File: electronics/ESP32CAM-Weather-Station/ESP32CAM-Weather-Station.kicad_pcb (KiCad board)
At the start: 4 copper layers, 100 x 100 mm, 93 parts, among them IC1 BME688, IC2 SGP41-D-R4, IC3 VEML7700-TT, IC4 BQ24093DGQR, IC5 BQ29707DSET, IC6 MCP3426A0T-E_SN, IC7 TPS63070RNMR, J1 B4B-PH-SM4-TB_LF__SN_, J10 Conn_01x02_Pin, J2 B4B-PH-SM4-TB_LF__SN_, J3 B4B-PH-SM4-TB_LF__SN_, J4 B4B-PH-SM4-TB_LF__SN_, J6 XT30UPB-M, J7 Conn_01x02_Pin, J8 Conn_01x02_Pin, J9 Conn_01x02_Pin, Q2 CSD16406Q3, Q3 CSD16406Q3, U1 ESP32-CAM, U2 TPS631000DRLR, U3 GDT25-07-S1-RP

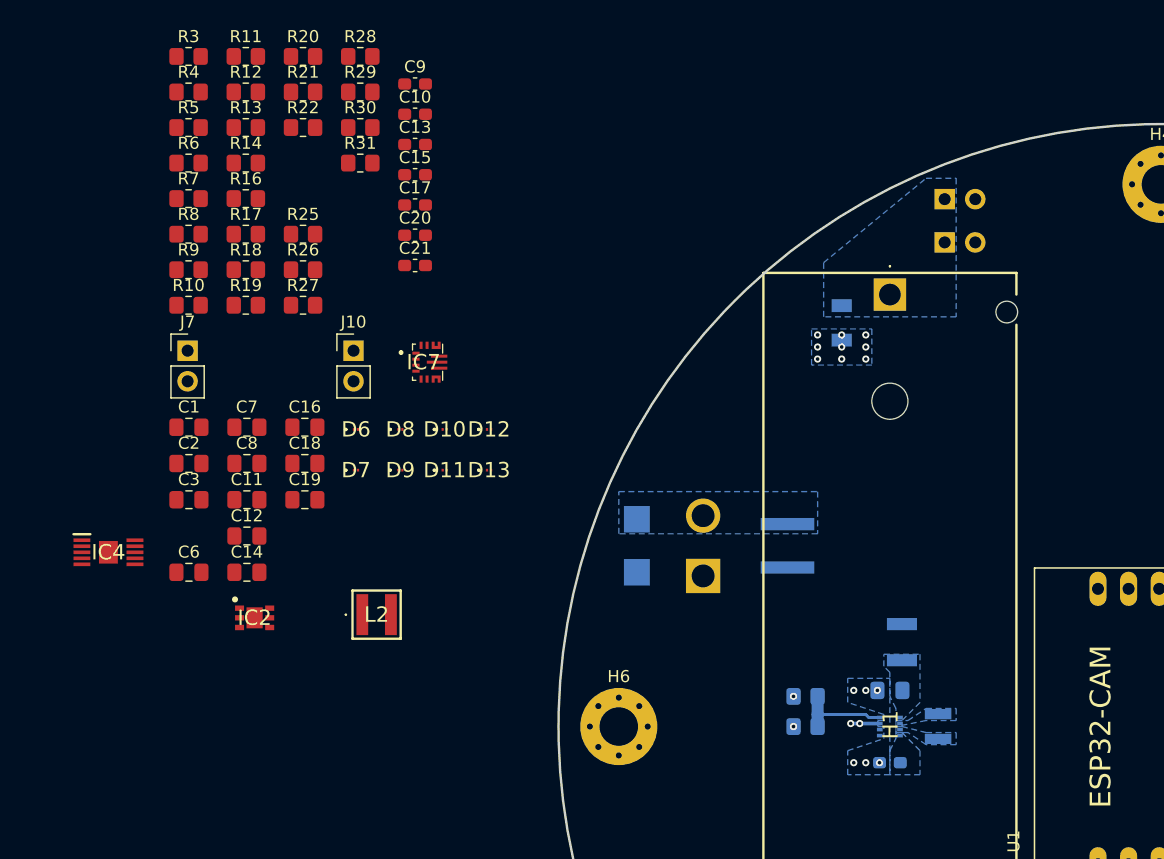
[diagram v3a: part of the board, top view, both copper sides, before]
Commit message: [WIP] Placed basic 5V regulator parts and moved 3V3 regulator so that output connects to the 3V3 plane.
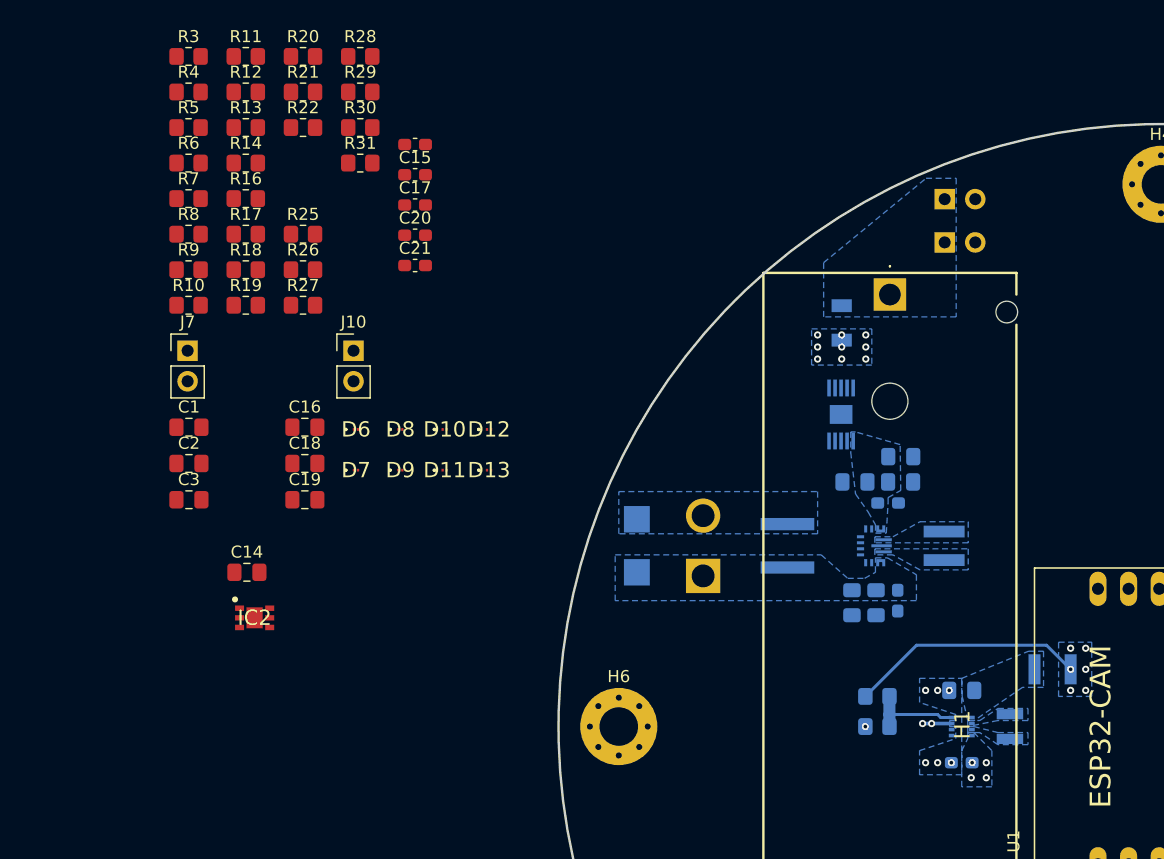
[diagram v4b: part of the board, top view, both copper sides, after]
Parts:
- C10, C11, C12, C6, C7, C8, C9, IC4, IC7, L2: moved to B.Cu
- moved IC4 61.9 mm to (123.5, 74.1), turned to 90 degrees
- moved C6 59.5 mm to (128.4, 79.7)
- moved C10 56.9 mm to (128.2, 89.5), turned to -90 degrees
- moved C7 54.3 mm to (128.4, 77.6)
- moved C11 52.9 mm to (126.3, 89.7), turned to -90 degrees
- moved C9 52.4 mm to (127.3, 81.5)
- moved C12 50.5 mm to (124.3, 89.7), turned to -90 degrees
- moved C8 50.5 mm to (124.6, 79.7), turned to 180 degrees
- moved L2 47.4 mm to (132.0, 85.0), turned to 90 degrees
- moved IC7 39.9 mm to (125.5, 85.0)
- moved F2 12.7 mm to (141.0, 95.2), turned to 180 degrees
- moved C4 5.96 mm to (133.5, 103.0)
- moved C5 5.96 mm to (133.5, 97.0)
- moved L1 5.96 mm to (137.5, 100.0)
- moved R23 5.96 mm to (126.5, 100.0)
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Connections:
- IC7 pad 16: (no net) -> +VSOLAR
- IC7 pad 17: (no net) -> +5V
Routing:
- net +3.3V: track 0.00 -> 19.6 mm, vias 1 -> 6
- net +VBAT: vias 9 -> 13
- added copper zone on B.Cu, net +3.3V
- added copper zone on B.Cu, net +5V
- added copper zone on B.Cu, net +VSOLAR
- added copper zone on B.Cu, net /5V_REG_L1
- added copper zone on B.Cu, net /5V_REG_L2

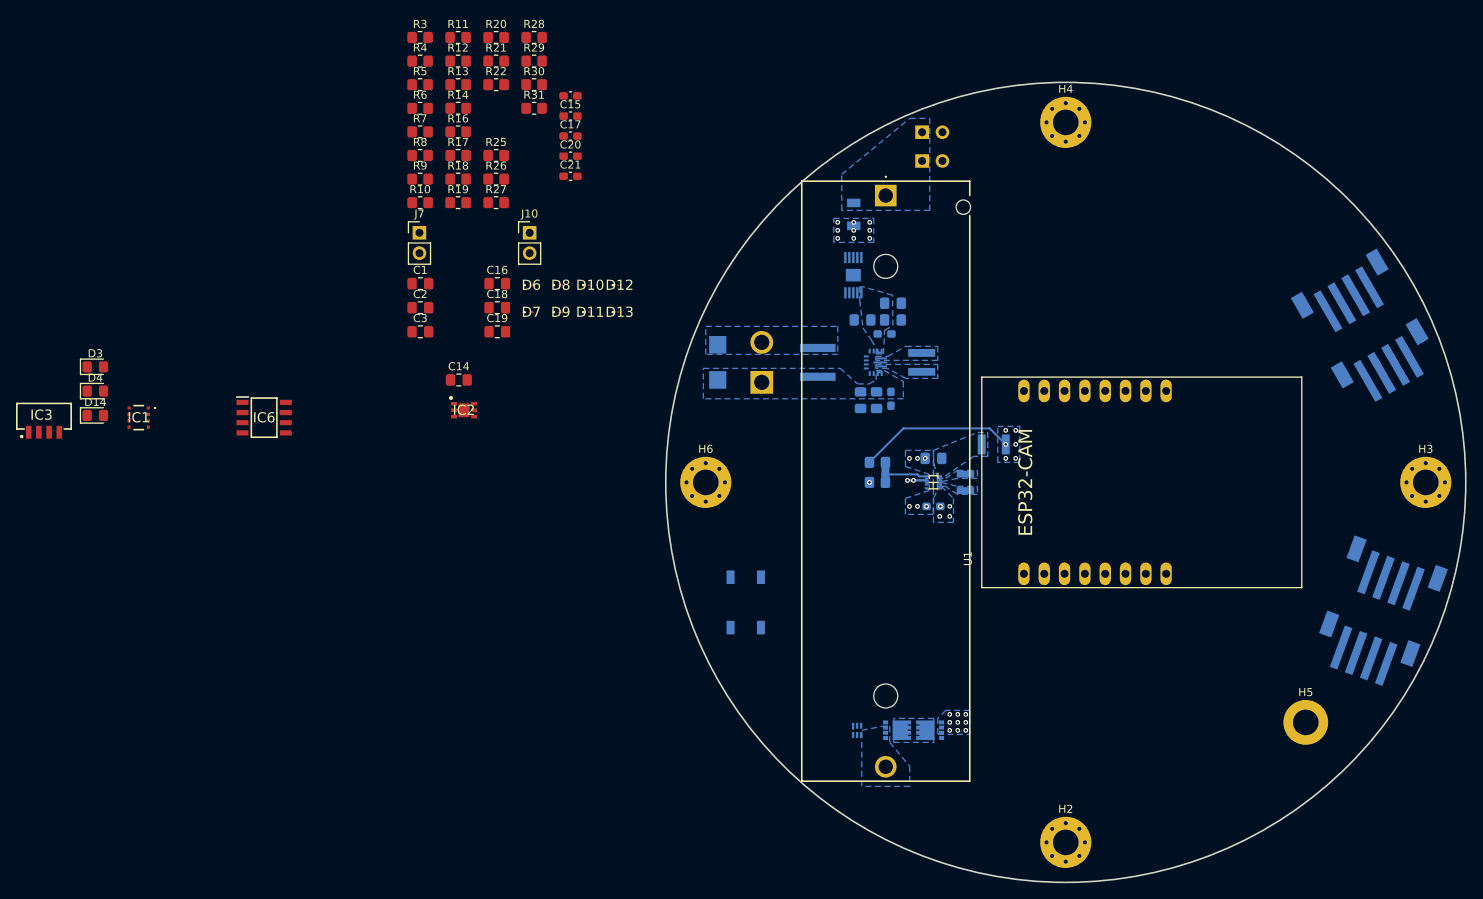
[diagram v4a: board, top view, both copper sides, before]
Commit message: [WIP] Placed all power components.
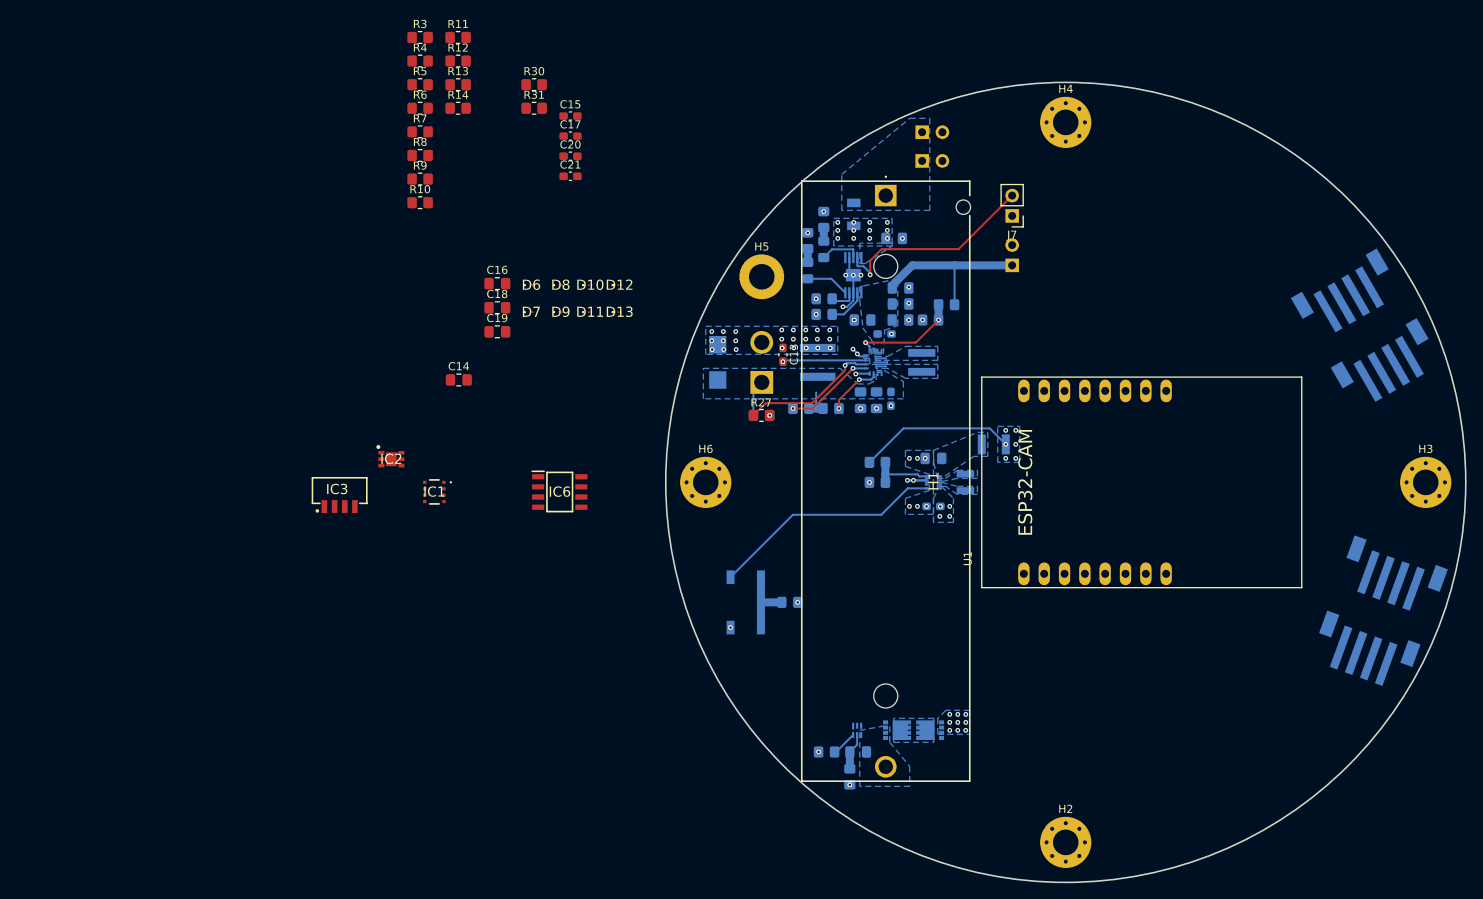
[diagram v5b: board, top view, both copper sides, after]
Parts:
- C1, C2, C3, D14, D4, J10, R16, R17, R18, R19, R20, R21, R22, R25, R26, R28, R29: moved to B.Cu
- D3: value LED_RED -> LED_GREEN; moved to B.Cu
- moved R16 94.3 mm to (123.0, 136.8), turned to -90 degrees
- moved D4 92.8 mm to (119.8, 70.9), turned to 90 degrees
- moved D3 89.9 mm to (117.8, 73.5), turned to 90 degrees
- moved H5 87.9 mm to (112.0, 74.3)
- moved R17 87.6 mm to (120.1, 133.7)
- moved D14 83.3 mm to (112.0, 91.6), turned to 180 degrees
- moved C1 80.1 mm to (124.0, 133.7)
- moved R22 74.4 mm to (115.5, 115.0), turned to 180 degrees
- moved J7 74.1 mm to (143.3, 66.7), turned to 180 degrees
- moved R28 61.4 mm to (135.1, 77.8), turned to 180 degrees
- moved J10 60.5 mm to (143.3, 72.9)
- moved C3 60.4 mm to (128.6, 69.5)
- moved C2 60.1 mm to (129.3, 75.7)
- moved R29 59.2 mm to (133.1, 79.7), turned to 180 degrees
- moved R20 53.7 mm to (119.8, 79.0), turned to 180 degrees
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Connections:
- C2 pad 1: +VBAT -> +5V
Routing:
- net /REG_EN: track 0.00 -> 29.1 mm
- net /CHG_TS: track 0.00 -> 26.1 mm, vias 0 -> 1
- net +5V: track 0.00 -> 21.3 mm
- net /5V_REG_PG: track 0.00 -> 17.2 mm, vias 0 -> 1
- net /5V_REG_FB: track 0.00 -> 13.5 mm, vias 0 -> 2
- net /5V_REG_PS_S: track 0.00 -> 11.2 mm, vias 0 -> 2
- net GND: track 2.41 -> 13.4 mm, vias 18 -> 63
- net /5V_REG_VAUX: track 0.00 -> 10.5 mm, vias 0 -> 1
- net Net-(S1-COM_1): track 0.00 -> 8.92 mm
- net +VSOLAR: track 0.00 -> 8.33 mm
- net /5V_REG_EN: track 0.00 -> 7.02 mm, vias 0 -> 2
- net /CHG_PG: track 0.00 -> 5.42 mm
- net /CHG_CHG: track 0.00 -> 5.14 mm
- net /ISET: track 0.00 -> 4.86 mm
- net /PROT_BAT: track 0.00 -> 4.60 mm
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
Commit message: [WIP] Completed most of the placement and routing.
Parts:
- added J5: Conn_01x04_Socket, Connector_PinHeader_2.54mm:PinHeader_1x04_P2.54mm_Vertical, B.Cu at (161.5, 127.9)
- C14, C15, C18, C19, C20, C21, IC1, IC2, IC6, R10, R11, R12, R13, R14, R3, R31, R4, R5, R6, R7, R8, R9: moved to B.Cu
- D14: value LED_RED -> LED_GREEN
- moved IC3 130.7 mm to (183.4, 131.3), turned to 135 degrees
- moved R30 124.1 mm to (182.2, 125.5), turned to -45 degrees
- moved C17 113.1 mm to (180.9, 121.3), turned to -45 degrees
- moved C16 111.2 mm to (179.4, 122.8), turned to 135 degrees
- moved IC2 108.2 mm to (169.0, 65.0), turned to 90 degrees
- moved C21 105.7 mm to (170.2, 128.3), turned to -90 degrees
- moved C20 105.5 mm to (167.8, 128.3), turned to -90 degrees
- moved IC1 103.6 mm to (169.0, 135.0), turned to 180 degrees
- moved R11 101.6 mm to (160.0, 98.5), turned to -90 degrees
- moved R10 93.8 mm to (156.9, 98.5), turned to -90 degrees
- moved R14 92.7 mm to (157.5, 93.5), turned to -90 degrees
- moved R9 92.2 mm to (154.0, 98.5), turned to 90 degrees
- moved R13 91.4 mm to (154.6, 93.5), turned to -90 degrees
- moved C19 91.3 mm to (167.9, 60.9), turned to 180 degrees
- moved R12 90.3 mm to (151.6, 93.5), turned to 90 degrees
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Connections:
- IC2 pad 3: /I2C_SDA -> unconnected-(IC2-SDA-Pad3)
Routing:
- net /I2C_SDA: track 0.00 -> 91.4 mm, vias 0 -> 1
- net /I2C_SCL: track 0.00 -> 85.3 mm, vias 0 -> 1
- net +3.3V: track 19.6 -> 50.4 mm, vias 6 -> 17
- net +VSOLAR: track 8.33 -> 27.4 mm
- net +VBAT: track 0.00 -> 10.5 mm, vias 20 -> 21
- net GND: track 13.4 -> 22.7 mm, vias 63 -> 81
- net /VSOLAR_SNS: track 0.00 -> 8.02 mm
- net /VBAT_SNS: track 0.00 -> 5.86 mm
- net /SGP41_VDD_TAP: track 0.00 -> 5.06 mm
- net Net-(IC3-VDD): track 0.00 -> 3.30 mm
- net Net-(R10-Pad2): track 0.00 -> 3.05 mm
- net Net-(R12-Pad2): track 0.00 -> 2.95 mm
- net Net-(R13-Pad2): track 0.00 -> 2.95 mm
- net Net-(R10-Pad1): track 0.00 -> 2.95 mm
- net Net-(R5-Pad1): track 0.00 -> 2.30 mm
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
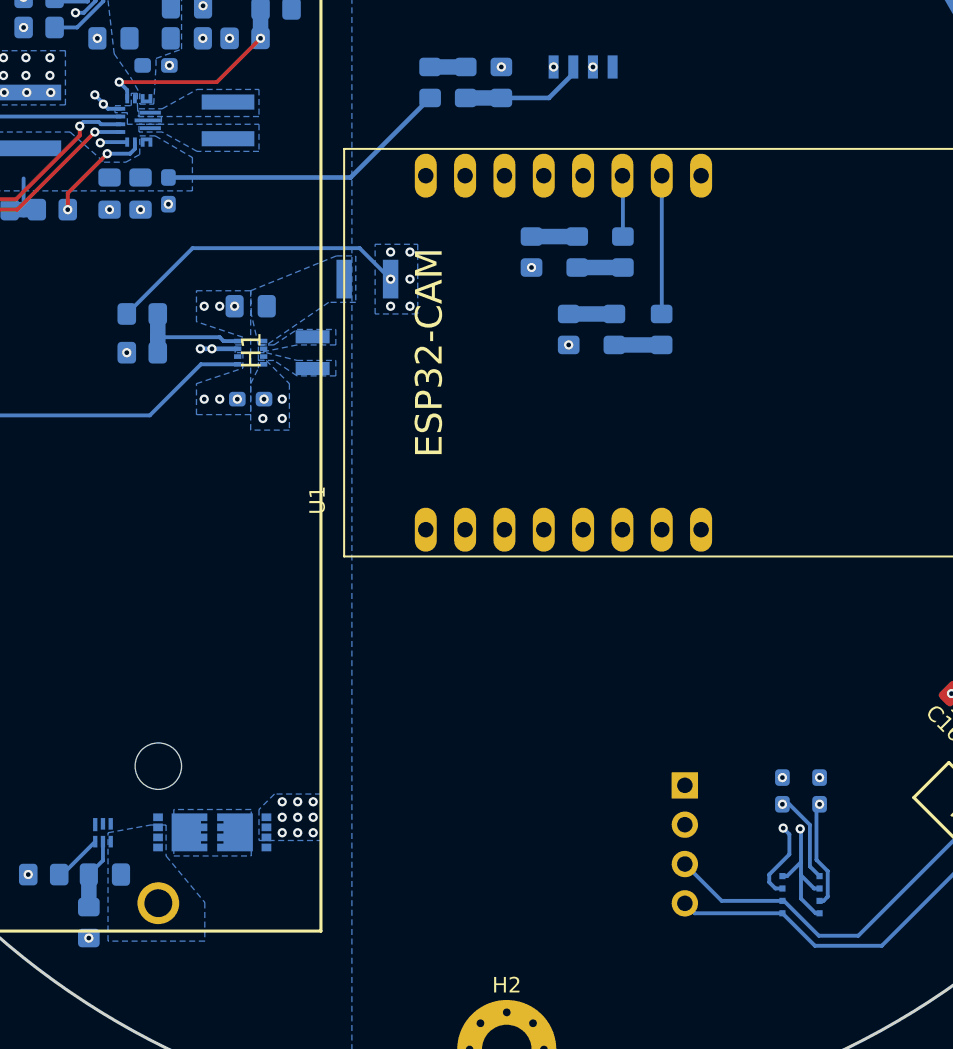
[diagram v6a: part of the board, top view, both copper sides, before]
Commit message: [WIP] Power stage routed. Created board cutouts for BME688.
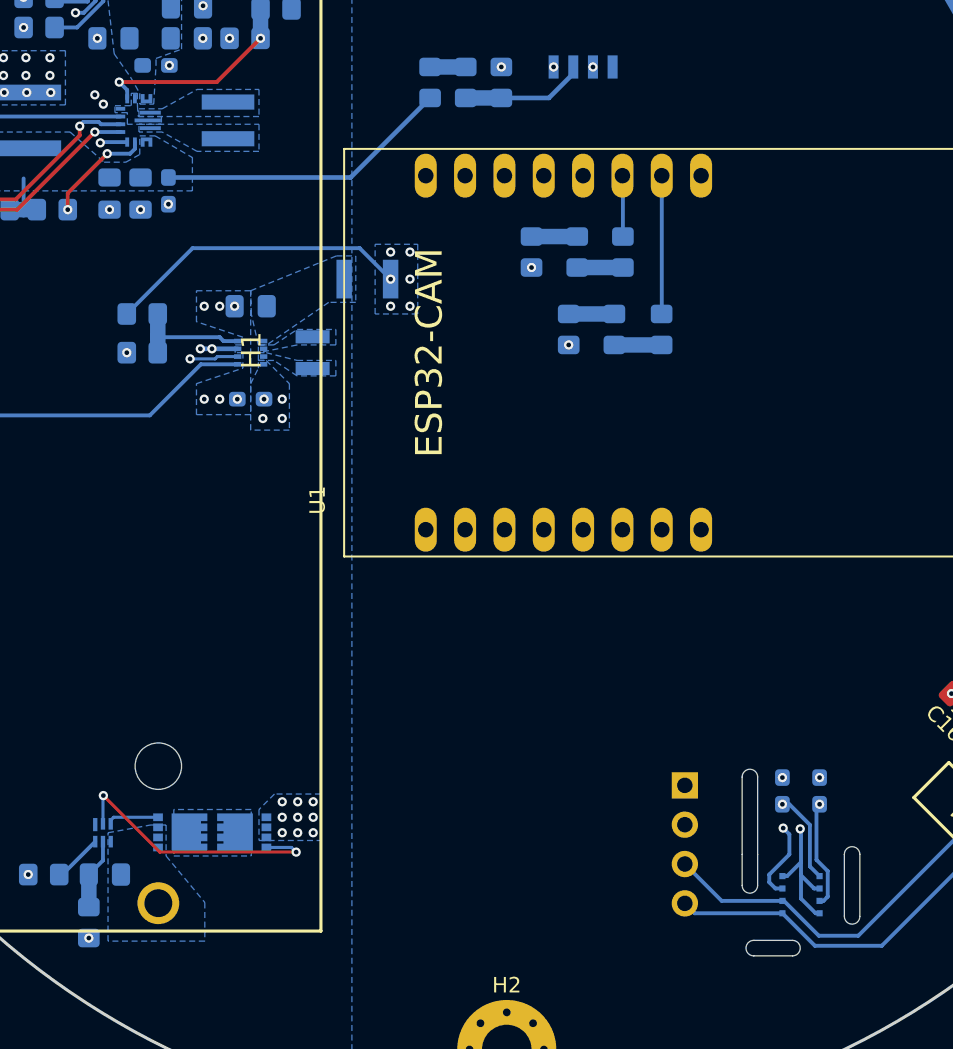
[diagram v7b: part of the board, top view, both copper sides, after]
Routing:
- net Net-(IC5-COUT): track 0.00 -> 17.8 mm, vias 0 -> 2
- net Net-(IC5-DOUT): track 0.00 -> 3.37 mm
- net +VBAT: track 10.5 -> 13.6 mm, vias 21 -> 22
- net GND: track 22.7 -> 20.7 mm
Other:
- outline, holes or cut-outs redrawn
